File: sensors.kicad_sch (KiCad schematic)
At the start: 26 parts, among them J2 Conn_01x02, J3 Conn_01x08, J4 Conn_01x04, Q27 PMOS, Q28 PMOS, U4 BMP280, U5 Si7020-A20, U6 QMA6100P, U7 ${SIM.PARAMS}, U8 ADS1243, U9 74HC138

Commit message: fix: 修复commit `38e8c9e`将元器件移动子原理图到造成的位号混乱
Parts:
- renumbered C40 to C36, C41 to C40, C36 to C41, J3 to J2, J2 to J3, R76 to R72, R74 to R73, R75 to R74, R73 to R75, R78 to R76, R81 to R77, R79 to R78, R80 to R79, R72 to R80, R82 to R81, R83 to R82, R77 to R83, U9 to U4, U4 to U5, U7 to U6, U5 to U7, U6 to U8, U8 to U9

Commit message: 分配MCU引脚，连接原理图，添加CAN收发器
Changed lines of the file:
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@@
+	(wire
+		(pts
+			(xy 260.35 110.49) (xy 264.16 110.49)
+		)
+		(stroke
+			(width 0)
+			(type default)
+		)
+	)
 	(wire
 		(pts
@@
 	(wire
 		(pts
+			(xy 260.35 113.03) (xy 264.16 113.03)
+		)
+		(stroke
+			(width 0)
+			(type default)
+		)
+	)
+	(wire
+		(pts
 			(xy 83.82 129.54) (xy 91.44 129.54)
 		)
@@
 	(wire
 		(pts
+			(xy 260.35 105.41) (xy 264.16 105.41)
+		)
+		(stroke
+			(width 0)
+			(type default)
+		)
+	)
+	(wire
+		(pts
 			(xy 78.74 113.03) (xy 78.74 114.3)
 		)
@@
 		(pts
 			(xy 163.83 59.69) (xy 163.83 60.96)
+		)
+		(stroke
+			(width 0)
+			(type default)
+		)
+	)
+	(wire
+		(pts
+			(xy 260.35 107.95) (xy 264.16 107.95)
 		)
 		(stroke
@@
 		)
 	)
+	(label "CS_AD"
+		(at 264.16 113.03 0)
+		(effects
+			(font
+				(size 1.27 1.27)
+			)
+			(justify left bottom)
+		)
+	)
+	(label "MISO"
+		(at 264.16 107.95 0)
+		(effects
+			(font
+				(size 1.27 1.27)
+			)
+			(justify left bottom)
+		)
+	)
 	(label "SCL"
 		(at 64.77 43.18 180)
@@
 		)
 	)
+	(label "MOSI"
+		(at 264.16 110.49 0)
+		(effects
+			(font
+				(size 1.27 1.27)
+			)
+			(justify left bottom)
+		)
+	)
 	(label "MISO"
 		(at 256.54 34.29 0)
+		(effects
+			(font
+				(size 1.27 1.27)
+			)
+			(justify left bottom)
+		)
+	)
+	(label "SCLK"
+		(at 264.16 105.41 0)
 		(effects
 			(font
@@
 		)
 	)
+	(hierarchical_label "MISO"
+		(shape output)
+		(at 260.35 107.95 180)
+		(effects
+			(font
+				(size 1.27 1.27)
+			)
+			(justify right)
+		)
+	)
 	(hierarchical_label "RTEMP_R1"
 		(shape input)
@@
 		)
 	)
+	(hierarchical_label "CS_AD"
+		(shape input)
+		(at 260.35 113.03 180)
+		(effects
+			(font
+				(size 1.27 1.27)
+			)
+			(justify right)
+		)
+	)
+	(hierarchical_label "MOSI"
+		(shape input)
+		(at 260.35 110.49 180)
+		(effects
+			(font
+				(size 1.27 1.27)
+			)
+			(justify right)
+		)
+	)
 	(hierarchical_label "RTEMP_R2"
 		(shape input)
@@
 		)
 	)
+	(hierarchical_label "SCLK"
+		(shape input)
+		(at 260.35 105.41 180)
+		(effects
+			(font
+				(size 1.27 1.27)
+			)
+			(justify right)
+		)
+	)

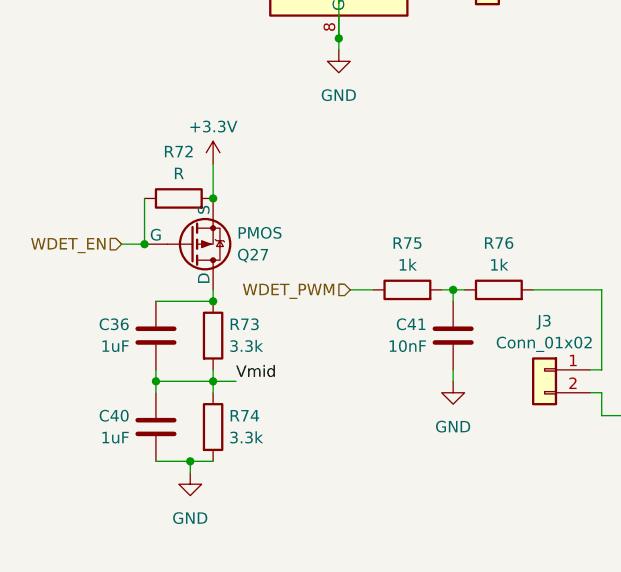
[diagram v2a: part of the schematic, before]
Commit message: 分配封装和在PCB上大致布局
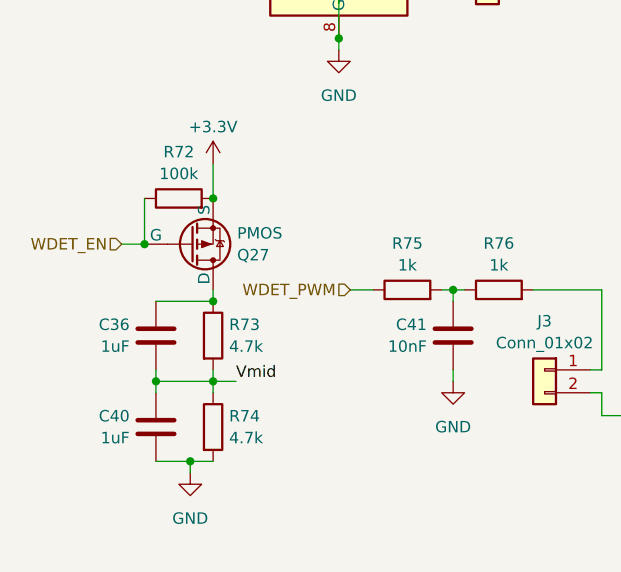
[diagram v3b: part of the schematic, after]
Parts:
- C36, C40, C41: footprint (none) -> Capacitor_SMD:C_0402_1005Metric
- J2: footprint (none) -> Connector_PinHeader_2.54mm:PinHeader_1x08_P2.54mm_Vertical
- J3: footprint (none) -> Connector_PinHeader_2.54mm:PinHeader_1x02_P2.54mm_Vertical
- J4: footprint (none) -> Connector_PinHeader_2.54mm:PinHeader_1x04_P2.54mm_Vertical
- Q27, Q28: footprint (none) -> Package_TO_SOT_SMD:SOT-23
- R72: value R -> 100k; footprint (none) -> Resistor_SMD:R_0402_1005Metric
- R73, R74: value 3.3k -> 4.7k; footprint (none) -> Resistor_SMD:R_0402_1005Metric
- R75, R76, R77, R78, R79, R80, R81, R82, R83: footprint (none) -> Resistor_SMD:R_0402_1005Metric
- U4: footprint (none) -> Package_SO:SSOP-16_4.4x5.2mm_P0.65mm
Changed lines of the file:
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@@
 			)
 		)
-		(property "Footprint" ""
+		(property "Footprint" "Resistor_SMD:R_0402_1005Metric"
 			(at 82.042 119.38 90)
 			(effects
@@
 			)
 		)
-		(property "Footprint" ""
+		(property "Footprint" "Resistor_SMD:R_0402_1005Metric"
 			(at 62.23 168.148 90)
 			(effects
@@
 			)
 		)
-		(property "Footprint" ""
+		(property "Footprint" "Resistor_SMD:R_0402_1005Metric"
 			(at 52.07 168.148 90)
 			(effects
@@
 			)
 		)
-		(property "Footprint" ""
+		(property "Footprint" "Package_TO_SOT_SMD:SOT-23"
 			(at 33.02 163.83 0)
 			(effects
@@
 			)
 		)
-		(property "Footprint" ""
+		(property "Footprint" "Package_TO_SOT_SMD:SOT-23"
 			(at 81.28 110.49 0)
 			(effects
@@
 			)
 		)
-		(property "Footprint" ""
+		(property "Footprint" "Resistor_SMD:R_0402_1005Metric"
 			(at 79.502 119.38 90)
 			(effects
@@
 			)
 		)
-		(property "Footprint" ""
+		(property "Footprint" "Package_SO:SSOP-16_4.4x5.2mm_P0.65mm"
 			(at 44.45 125.73 0)
 			(effects
@@
 			)
 		)
-		(property "Value" "3.3k"
+		(property "Value" "4.7k"
 			(at 32.258 172.6621 0)
 			(effects
@@
 			)
 		)
-		(property "Footprint" ""
+		(property "Footprint" "Resistor_SMD:R_0402_1005Metric"
 			(at 28.702 171.45 90)
 			(effects
@@
 			)
 		)
-		(property "Footprint" ""
+		(property "Footprint" "Resistor_SMD:R_0402_1005Metric"
 			(at 84.582 119.38 90)
 			(effects
@@
 			)
 		)
-		(property "Footprint" ""
+		(property "Footprint" "Connector_PinHeader_2.54mm:PinHeader_1x02_P2.54mm_Vertical"
 			(at 67.31 175.26 0)
 			(effects
@@
 			)
 		)
-		(property "Footprint" ""
+		(property "Footprint" "Capacitor_SMD:C_0402_1005Metric"
 			(at 25.0952 167.64 0)
 			(effects
@@
 			)
 		)
-		(property "Footprint" ""
+		(property "Footprint" "Connector_PinHeader_2.54mm:PinHeader_1x08_P2.54mm_Vertical"
 			(at 60.96 123.19 0)
 			(effects
@@
 			)
 		)
-		(property "Footprint" ""
+		(property "Footprint" "Capacitor_SMD:C_0402_1005Metric"
 			(at 58.1152 167.64 0)
 			(effects
@@
 			)
 		)
-		(property "Footprint" ""
+		(property "Footprint" "Resistor_SMD:R_0402_1005Metric"
 			(at 81.28 182.118 90)
 			(effects
@@
 			)
 		)
-		(property "Footprint" ""
+		(property "Footprint" "Capacitor_SMD:C_0402_1005Metric"
 			(at 25.0952 177.8 0)
 			(effects
@@
 			)
 		)
-		(property "Footprint" ""
+		(property "Footprint" "Resistor_SMD:R_0402_1005Metric"
 			(at 74.93 104.648 90)
 			(effects
@@
 			)
 		)
-		(property "Footprint" ""
+		(property "Footprint" "Resistor_SMD:R_0402_1005Metric"
 			(at 95.25 187.198 90)
 			(effects
@@
 			)
 		)
-		(property "Footprint" ""
+		(property "Footprint" "Resistor_SMD:R_0402_1005Metric"
 			(at 76.962 119.38 90)
 			(effects
@@
 			)
 		)
-		(property "Value" "3.3k"
+		(property "Value" "4.7k"
 			(at 32.258 182.8221 0)
 			(effects
@@
 			)
 		)
-		(property "Footprint" ""
+		(property "Footprint" "Resistor_SMD:R_0402_1005Metric"
 			(at 28.702 181.61 90)
 			(effects
@@
 			)
 		)
-		(property "Footprint" ""
+		(property "Footprint" "Connector_PinHeader_2.54mm:PinHeader_1x04_P2.54mm_Vertical"
 			(at 83.82 138.43 0)
 			(effects
@@
 			)
 		)
-		(property "Value" "R"
+		(property "Value" "100k"
 			(at 26.67 153.4738 90)
 			(effects
@@
 			)
 		)
-		(property "Footprint" ""
+		(property "Footprint" "Resistor_SMD:R_0402_1005Metric"
 			(at 26.67 157.988 90)
 			(effects

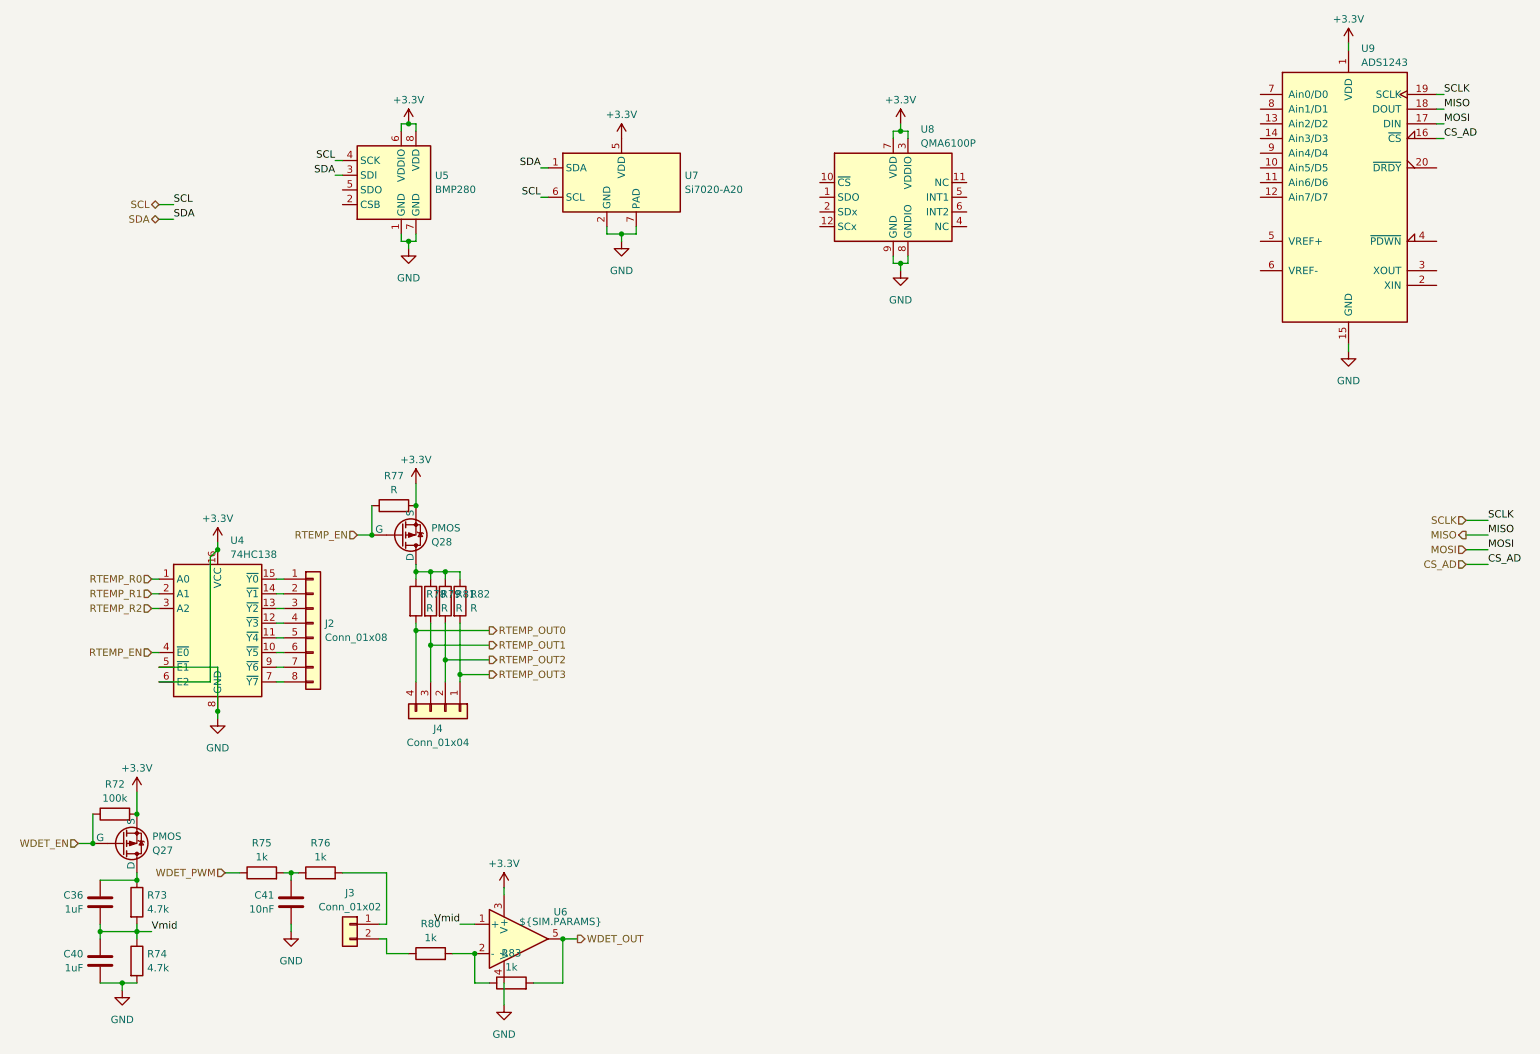
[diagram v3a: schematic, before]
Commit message: 分配封装，添加RS485通信接口，调整布局，传感器连接到独立MCU上
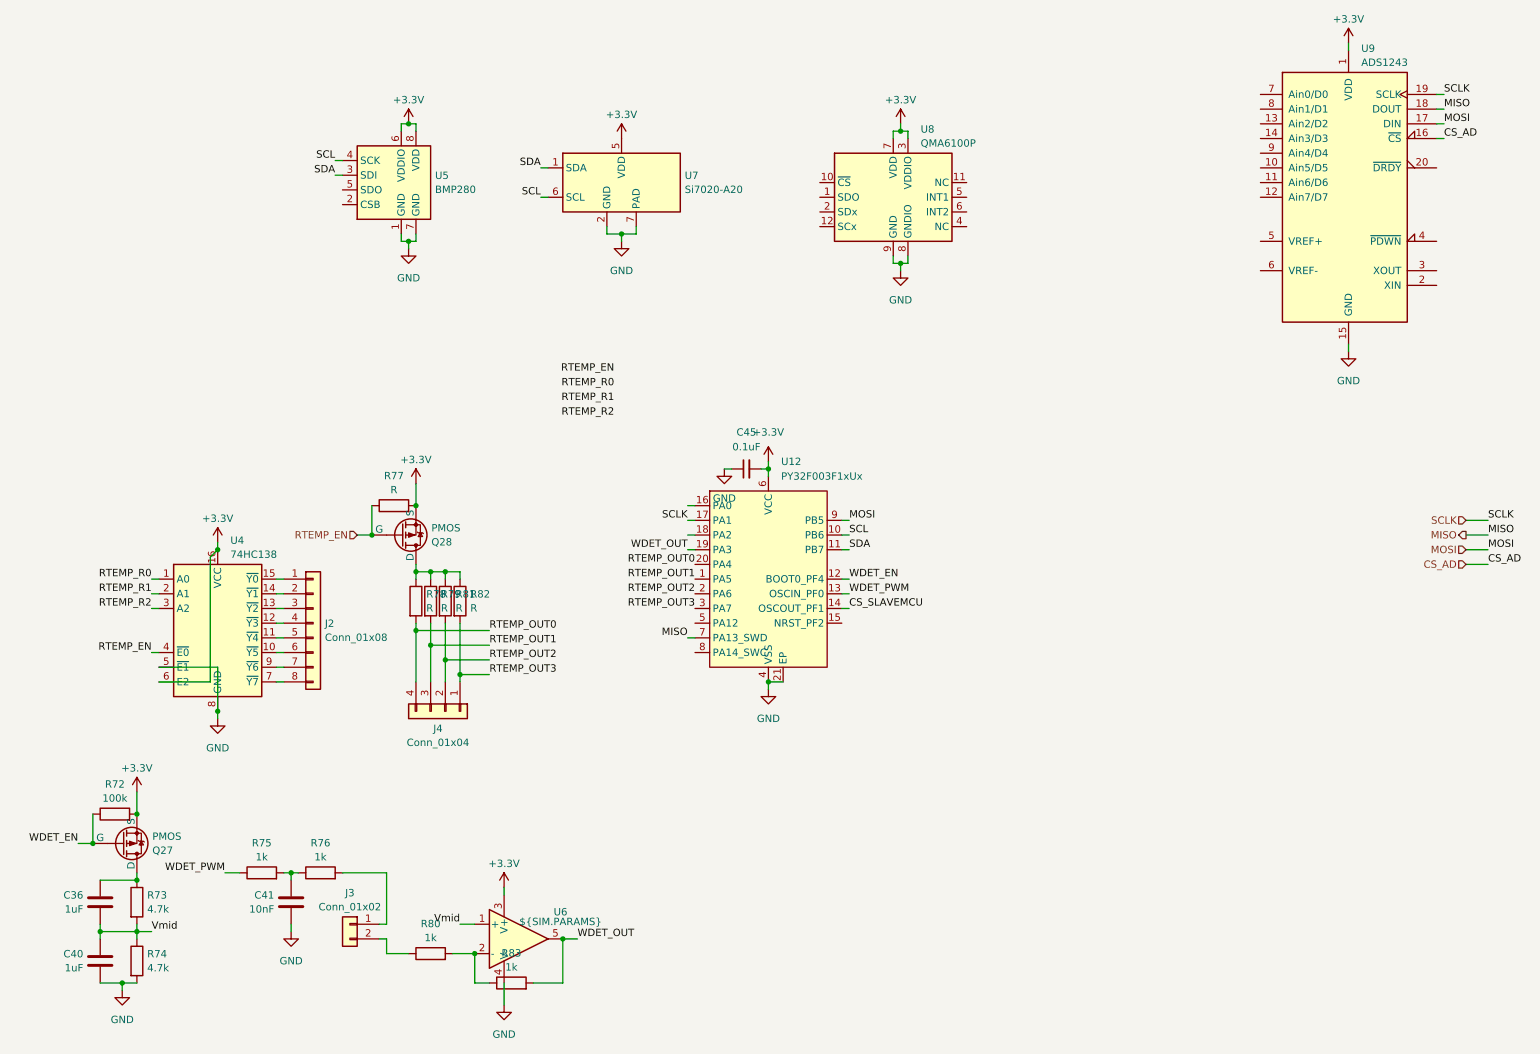
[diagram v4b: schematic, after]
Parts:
- added C45: 0.1uF, Capacitor_SMD:C_0402_1005Metric, symbol Device:C_Small
- added U12: PY32F003F1xUx, Package_DFN_QFN:QFN-20-1EP_3x3mm_P0.4mm_EP1.65x1.65mm, symbol project_syms:PY32F003F1xUx
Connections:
- net +3.3V: now also C45.2, U12.6 (VCC)
- net GND: now also C45.1, U12.21 (EP), U12.4 (VSS)
- net MISO: now also U12.7 (PA13_SWD)
- net MOSI: now also U12.9 (PB5)
- net RTEMP_OUT0: now also U12.20 (PA4)
- net RTEMP_OUT1: now also U12.1 (PA5)
- net RTEMP_OUT2: now also U12.2 (PA6)
- net RTEMP_OUT3: now also U12.3 (PA7)
- net SCL: now also U12.10 (PB6)
- net SCLK: now also U12.17 (PA1)
- net SDA: now also U12.11 (PB7)
- net WDET_EN: now also U12.12 (BOOT0_PF4)
- net WDET_OUT: now also U12.19 (PA3)
- net WDET_PWM: now also U12.13 (OSCIN_PF0)
- new net CS_SLAVEMCU: U12.14 (OSCOUT_PF1)

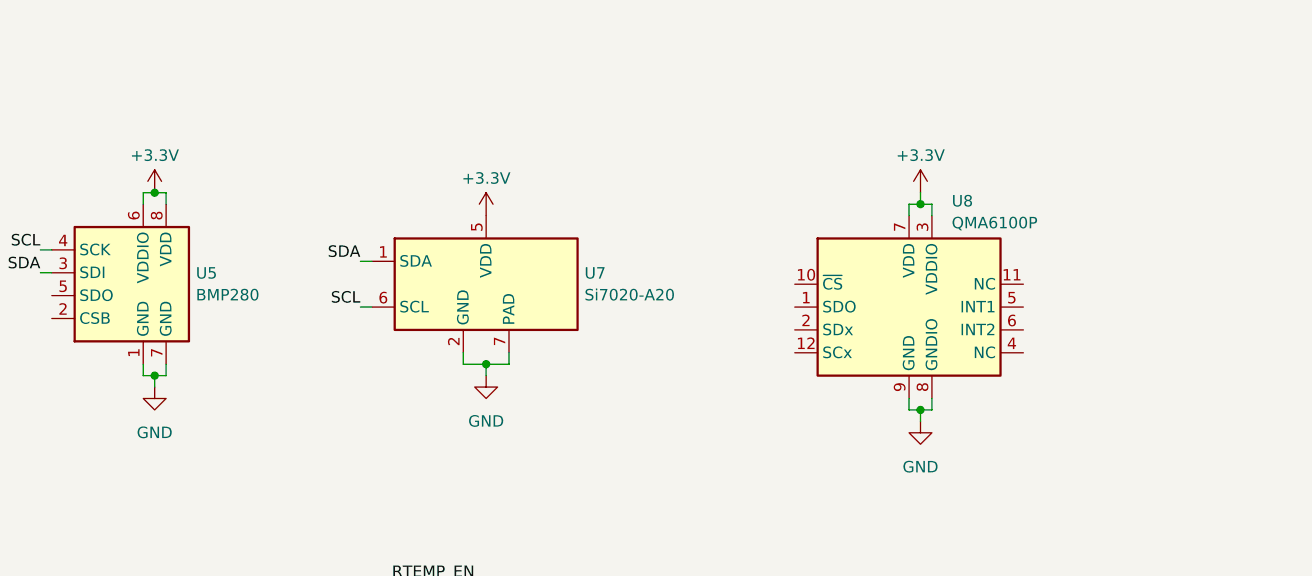
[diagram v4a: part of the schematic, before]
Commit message: 修改电源电路
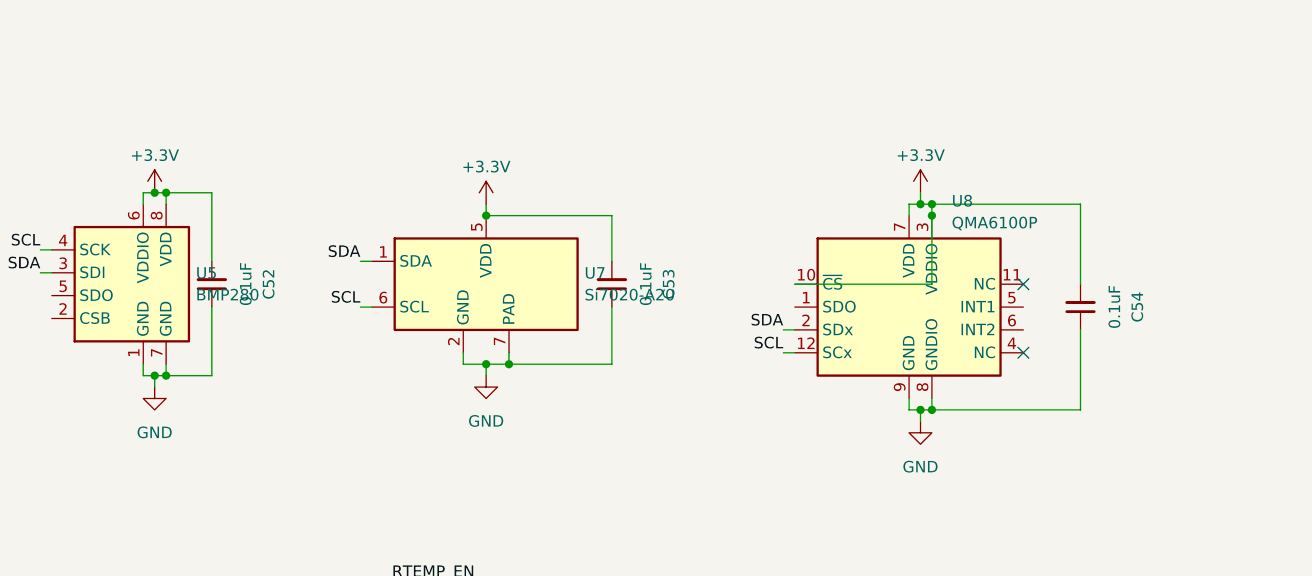
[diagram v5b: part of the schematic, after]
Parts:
- added C52, C53, C54: 0.1uF, Capacitor_SMD:C_0402_1005Metric, symbol Device:C_Small
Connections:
- net +3.3V: now also U8.10 (~{CS}), C52.2, C53.2, C54.2
- net GND: now also C52.1, C53.1, C54.1
- net SCL: now also U8.12 (SCx)
- net SDA: now also U8.2 (SDx)
- no-connect marks 0 -> 2
